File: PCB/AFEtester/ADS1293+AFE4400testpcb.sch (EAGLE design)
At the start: 47 parts, among them IC1 ADS1293, J1 POWER_JACK, U2 TPS61093DSKT, Y1 4.096MHz

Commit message: afe4400 pcb stuff
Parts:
- added 3V3-POWER-TESTPOINT1, 3V3-POWER-TESTPOINT2: (no value), SparkFun-Connectors:CONN_02
- added C16: 1nF, SparkFun-Capacitors:1.0NF/1000PF-0603-50V-10%
- added C17, C18, C19, C20, C22, C23, C24: 10uF, SparkFun-Retired:10UF-TANT
- added C21, C27: 10nF, SparkFun-Capacitors:10NF-0603-50V-10%
- added C25, C29, C30: 0.1uF, SparkFun-Capacitors:0.1UF-0603-25V-5%
- added C26: 1.0uF, SparkFun-Capacitors:1.0UF-0805-25V-10%
- added C28, C31: 2.2uF, SparkFun-Capacitors:2.2UF-0805-25V-(+80/-20%)
- added C32, C33: 18pF, SparkFun-Capacitors:18PF-0603-50V-5%
- added D1: GREEN, SparkFun-LED:LED-GREEN1206
- added D2, D3: BAV99S, nxp_60:BAV99S
- added FRAME2: FRAME-LEDGER, SparkFun-Aesthetics:FRAME-LEDGER
- added IC2: LP3878MR-ADJ_NOPB, LP3878MR-ADJ_NOPB:LP3878MR-ADJ_NOPB
- added J3: (no value), SparkFun-Connectors:DB9FEMALE
- added J4: (no value), SparkFun-Connectors:CONN_08"
- added J5: (no value), SparkFun-Connectors:CONN_04
- added L2, L3, L4: 3.3µH/±20%/450mA, SparkFun-Coils:INDUCTOR-0805-3.3UH
- added R18, R29: 1k, SparkFun-Resistors:1KOHM-0603-1/10W-1%
- added R19: 4.7k, SparkFun-Resistors:4.7KOHM-0603-1/10W-1%
- added R20, R21, R24, R25, R26, R27, R28, R30, R31, R32, R33, R34, R35: 0, SparkFun-Resistors:0OHM-0603-1/10W-5%
- added R22: 75k, SparkFun-Resistors:75KOHM-0603-1/10W-1%
- added R23: 47k, SparkFun-Resistors:47KOHM-0603-1/10W-1%
- added R36: 10, SparkFun-Resistors:10OHM-0603-1/10W-1%
- added R37: 10k, SparkFun-Resistors:10KOHM-0603-1/10W-1%
- added R38, R39, R40, R41, R42, R43: 130, SparkFun-Resistors:330OHM-0603-1/10W-1%
- added S2: MOMENTARY-SWITCH-SPST-PTH-6.0MM, SparkFun-Switches:MOMENTARY-SWITCH-SPST-PTH-6.0MM
- added U3: AFE4400_RHA_40, AFE4400:AFE4400_RHA_40
- added Y2: 8MHz, SparkFun-Clocks:CRYSTAL-8MHZSMD-5X3.2
- C13: device SparkFun-Capacitors:10UF-0805-10V-10% -> SparkFun-Retired:10UF-TANT
- C14, C15: value 0.1uF -> 10nF; device SparkFun-Capacitors:0.1UF-0603-25V-(+80/-20%) -> SparkFun-Capacitors:10NF-0603-50V-10%
- L1: value LPS3010-102MRC -> 3.3µH/±20%/450mA; device LPS3010-102MRC:LPS3010-102MRC -> SparkFun-Coils:INDUCTOR-0805-3.3UH
- R17: value 0 -> 2.55k; device SparkFun-Resistors:0OHM-0603-1/10W-5% -> SparkFun-Resistors:2.55KOHM-0603-1/10W-1%
- U2: value TPS61093DSKT -> TPS7A4901DGNR; device Texas Instruments_By_element14_Batch_1:TPS61093DSKT -> Texas Instruments_By_element14_Batch_1:TPS7A4901DGNR
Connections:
- removed net C: COMM-CONN.6, IC1.SCLK
- removed net VCC: C13.1, R16.1
- new net ADC_RDY: J4.5, U3.ADC_RDY
- new net AFE_PDN: J4.8, U3.AFE_*PDN
- new net CLKOUT_AFE: J4.2, R36.2
- new net DIAG_END: J4.7, U3.DIAG_END
- new net LED_ALM: J4.6, U3.LED_ALM
- new net LED_DRV_SUP: C26.1, D3-1.K2, D3-2.K2, J5.1, R20.2, U3.LED_DRV_SUP, U3.LED_DRV_SUP_2
- new net N$21: 3V3-POWER-TESTPOINT1.2, C16.1, IC2.OUT, R17.2
- new net N$22: C14.1, U2.NR/SS
- new net N$23: C19.+, L1.2, R20.1
- new net N$24: C20.+, L2.2, R21.1
- new net N$25: C13.+, R26.1, U2.EN, U2.IN
- new net N$26: 3V3-POWER-TESTPOINT2.2, C21.1, R22.2, U2.OUT
- new net N$27: C21.2, R22.1, R23.2, U2.FB
- new net N$28: C23.+, L3.2, R27.1
- new net N$29: C17.+, IC2.!SHUTDOWN, IC2.IN, R25.1
- new net N$30: C24.+, L4.2, R28.1
- new net N$31: C28.2, U3.BG
- new net N$32: C31.1, U3.TX_REF
- new net N$33: R32.2, U3.TXN
- new net N$34: R29.2, U3.VCM
- new net N$36: R31.2, U3.INN
- new net N$37: R30.2, U3.INP
- new net N$38: D2-2.K1A2, J3.5, R31.1
- new net N$39: D2-1.K1A2, J3.9, R30.1
- new net N$40: R33.2, U3.TXP
- new net N$41: D3-1.K1A2, J3.3, R32.1
- new net N$42: D3-2.K1A2, J3.2, R33.1
- new net N$43: C32.2, R34.2, Y2.1
- new net N$44: C33.1, R35.1, Y2.2
- new net N$45: R36.1, U3.CLKOUT
- new net N$46: R37.2, S2.2, U3.*RESET
- new net N$48: R35.2, U3.XOUT
- new net N$49: R38.1, U3.DNC
- new net N$50: R42.1, U3.DNC_2
- new net N$52: R41.1, U3.DNC_3
- new net N$53: R40.1, U3.DNC_4
- new net N$54: R39.1, U3.DNC_5
- new net N$55: R38.2
- new net N$56: R39.2
- new net N$57: R40.2
- new net N$58: R41.2
- new net N$59: R42.2
- new net PD_ALM: J4.4, U3.PD_ALM
- new net RX_ANA_SUP: C30.1, D2-1.K2, D2-2.K2, J5.4, R28.2, U3.RX_ANA_SUP, U3.RX_ANA_SUP_2
- new net RX_DIG_SUP: C29.1, J5.3, R27.2, R37.1, U3.RX_DIG_SUP
- new net RX_SUP: 3V3-POWER-TESTPOINT2.1, C22.+, L3.1, L4.1
- new net SCLK: COMM-CONN.6, IC1.SCLK, U3.SCLK
- new net STE: J4.1, U3.SPISTE
- new net TX_CTRL_SUP: C25.1, J5.2, R21.2, U3.TX_CTRL_SUP
- new net VCM_SHIELD: C27.1, R29.1
- new net XIN_MSP: J4.3, R34.1, U3.XIN
- net +5V: now also D1.A, R25.2, R26.2
- net GND: now also C13.-, C14.2, C15.2, C17.-, C18.-, C19.-, C20.-, C22.-, C23.-, C24.-, C25.2, C26.2, C27.2, C28.1, C29.2, C30.2, C31.2, C32.1, C33.2, D2-1.A1, D2-2.A1, D3-1.A1, D3-2.A1, IC2.EP, IC2.GND, IC2.NC_1, J3.7, R16.1, R16.2, R18.1, R19.1, R23.1, R24.1, R24.2, R43.1, S2.1, U2.EP, U3.EPAD, U3.LED_DRV_GND, U3.LED_DRV_GND_2, U3.LED_DRV_GND_3, U3.RX_ANA_GND, U3.RX_ANA_GND_2, U3.RX_ANA_GND_3, U3.RX_DIG_GND, U3.RX_DIG_GND_2, U3.VSS; no longer C13.2
- net MISO: now also U3.SPISOMI
- net MOSI: now also U3.SPISIMO
- net N$18: now also 3V3-POWER-TESTPOINT1.1, C18.+, L1.1, L2.1; no longer R17.2, U2.EN
- net N$19: now also C16.2, IC2.ADJ, R18.2; no longer R16.2, U2.VIN
- net N$20: now also C15.1, IC2.BYP; no longer C15.2, U2.CP2
- net N$4: now also D1.C, R19.2; no longer C15.1, U2.CP1
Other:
- note added: "2.7kR will be better"
- note added: "we can also try 1uH"
- moved on the sheet: C14, C15, R16, R17

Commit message: almost complete AFE PCB
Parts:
- removed FRAME2: FRAME-LEDGER, SparkFun-Aesthetics:FRAME-LEDGER
- J5: device SparkFun-Connectors:CONN_04 -> SparkFun-Connectors:CONN_05
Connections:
- net GND: now also J5.5; no longer R43.1
- net LED_DRV_SUP: now also J5.3; no longer J5.1
- net N$31: now also R43.1
- net RX_ANA_SUP: now also J5.1; no longer J5.4
- net RX_DIG_SUP: now also J5.2; no longer J5.3
- net TX_CTRL_SUP: now also J5.4; no longer J5.2
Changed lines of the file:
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@@
 <part name="SUPPLY32" library="supply2" library_urn="urn:adsk.eagle:library:372" deviceset="GND" device=""/>
 <part name="R43" library="SparkFun-Resistors" deviceset="330OHM" device="-0603-1/10W-1%" value="130"/>
-<part name="FRAME2" library="SparkFun-Aesthetics" deviceset="FRAME-LEDGER" device=""/>
 <part name="J4" library="SparkFun-Connectors" deviceset="CONN_08" device="&quot;"/>
-<part name="J5" library="SparkFun-Connectors" deviceset="CONN_04" device=""/>
+<part name="J5" library="SparkFun-Connectors" deviceset="CONN_05" device=""/>
+<part name="SUPPLY33" library="supply2" library_urn="urn:adsk.eagle:library:372" deviceset="GND" device=""/>
 </parts>
 <sheets>
@@
 <instance part="SUPPLY32" gate="GND" x="320.04" y="53.34"/>
 <instance part="R43" gate="G$1" x="447.04" y="106.68"/>
-<instance part="FRAME2" gate="G$1" x="294.64" y="2.54"/>
-<instance part="FRAME2" gate="G$2" x="624.84" y="2.54"/>
 <instance part="J4" gate="G$1" x="576.58" y="251.46"/>
-<instance part="J5" gate="G$1" x="576.58" y="208.28"/>
+<instance part="J5" gate="G$1" x="576.58" y="210.82"/>
+<instance part="SUPPLY33" gate="GND" x="594.36" y="220.98"/>
 </instances>
 <busses>
@@
 <pinref part="SUPPLY23" gate="GND" pin="GND"/>
 <wire x1="441.96" y1="101.6" x2="449.58" y2="101.6" width="0.1524" layer="91"/>
-<wire x1="441.96" y1="101.6" x2="441.96" y2="106.68" width="0.1524" layer="91"/>
-<junction x="441.96" y="101.6"/>
-<pinref part="R43" gate="G$1" pin="1"/>
 </segment>
 <segment>
@@
 <wire x1="320.04" y1="68.58" x2="320.04" y2="55.88" width="0.1524" layer="91"/>
 <pinref part="SUPPLY32" gate="GND" pin="GND"/>
+</segment>
+<segment>
+<pinref part="J5" gate="G$1" pin="5"/>
+<wire x1="584.2" y1="215.9" x2="586.74" y2="215.9" width="0.1524" layer="91"/>
+<wire x1="586.74" y1="215.9" x2="586.74" y2="226.06" width="0.1524" layer="91"/>
+<wire x1="586.74" y1="226.06" x2="594.36" y2="226.06" width="0.1524" layer="91"/>
+<pinref part="SUPPLY33" gate="GND" pin="GND"/>
+<wire x1="594.36" y1="226.06" x2="594.36" y2="223.52" width="0.1524" layer="91"/>
 </segment>
 </net>
@@
 </segment>
 <segment>
-<pinref part="J5" gate="G$1" pin="1"/>
-<wire x1="581.66" y1="205.74" x2="586.74" y2="205.74" width="0.1524" layer="91"/>
-<label x="586.74" y="205.74" size="1.778" layer="95" xref="yes"/>
+<pinref part="J5" gate="G$1" pin="3"/>
+<wire x1="584.2" y1="210.82" x2="596.9" y2="210.82" width="0.1524" layer="91"/>
+<label x="596.9" y="210.82" size="1.778" layer="95" xref="yes"/>
 </segment>
 </net>
@@
 </segment>
 <segment>
-<pinref part="J5" gate="G$1" pin="2"/>
-<wire x1="581.66" y1="208.28" x2="586.74" y2="208.28" width="0.1524" layer="91"/>
-<label x="586.74" y="208.28" size="1.778" layer="95" xref="yes"/>
+<pinref part="J5" gate="G$1" pin="4"/>
+<wire x1="584.2" y1="213.36" x2="596.9" y2="213.36" width="0.1524" layer="91"/>
+<label x="596.9" y="213.36" size="1.778" layer="95" xref="yes"/>
 </segment>
 </net>
@@
 </segment>
 <segment>
-<pinref part="J5" gate="G$1" pin="3"/>
-<wire x1="581.66" y1="210.82" x2="586.74" y2="210.82" width="0.1524" layer="91"/>
-<label x="586.74" y="210.82" size="1.778" layer="95" xref="yes"/>
+<pinref part="J5" gate="G$1" pin="2"/>
+<wire x1="584.2" y1="208.28" x2="596.9" y2="208.28" width="0.1524" layer="91"/>
+<label x="596.9" y="208.28" size="1.778" layer="95" xref="yes"/>
 </segment>
 </net>
@@
 </segment>
 <segment>
-<pinref part="J5" gate="G$1" pin="4"/>
-<wire x1="581.66" y1="213.36" x2="586.74" y2="213.36" width="0.1524" layer="91"/>
-<label x="586.74" y="213.36" size="1.778" layer="95" xref="yes"/>
+<pinref part="J5" gate="G$1" pin="1"/>
+<wire x1="584.2" y1="205.74" x2="596.9" y2="205.74" width="0.1524" layer="91"/>
+<label x="596.9" y="205.74" size="1.778" layer="95" xref="yes"/>
 </segment>
 </net>
@@
 <pinref part="C28" gate="G$1" pin="2"/>
 <wire x1="447.04" y1="93.98" x2="441.96" y2="93.98" width="0.1524" layer="91"/>
-</segment>
-</net>
+<pinref part="R43" gate="G$1" pin="1"/>
+<wire x1="441.96" y1="106.68" x2="436.88" y2="106.68" width="0.1524" layer="91"/>
+<wire x1="436.88" y1="106.68" x2="436.88" y2="93.98" width="0.1524" layer="91"/>
+<wire x1="436.88" y1="93.98" x2="441.96" y2="93.98" width="0.1524" layer="91"/>
+<junction x="441.96" y="93.98"/>
+</segment>
+</net>

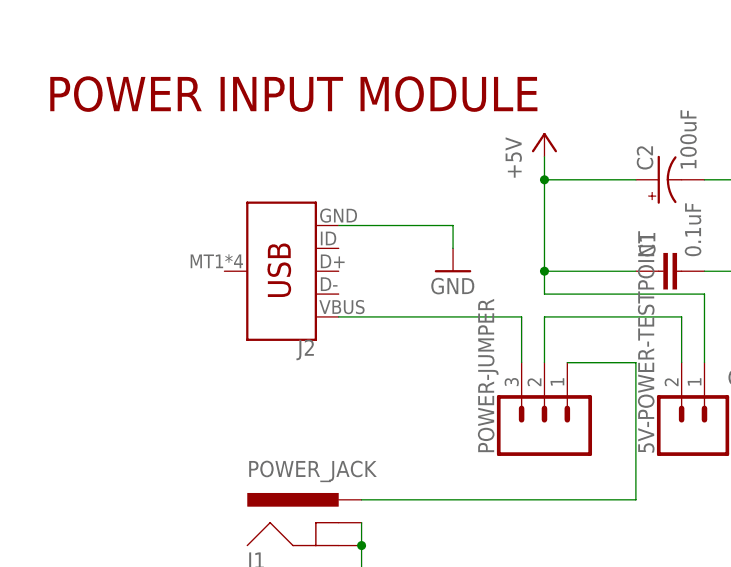
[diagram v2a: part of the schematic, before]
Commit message: Finishing ADS&AFE joint test pcb
exporting gerber
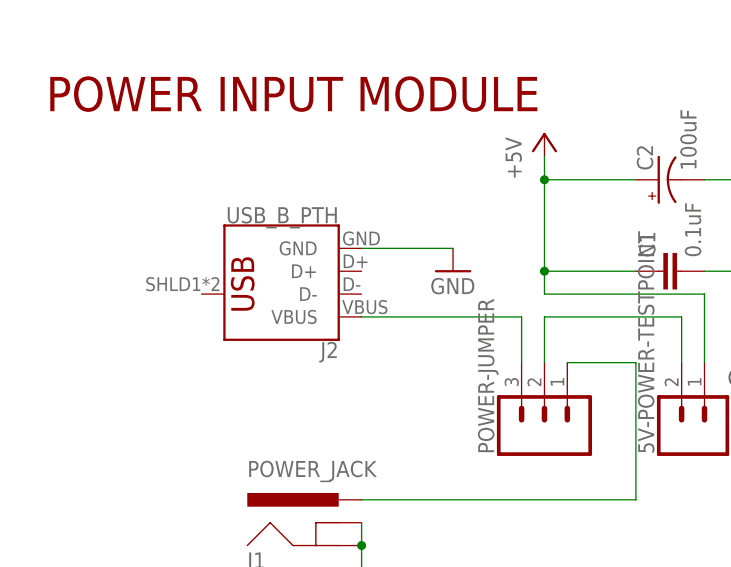
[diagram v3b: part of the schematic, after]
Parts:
- J2: value (none) -> USB_B_PTH; device SparkFun-Connectors:USB_MICRO-B_SMT -> SparkFun-Connectors:USB_B_PTH
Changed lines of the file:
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@@
 <part name="GND1" library="supply1" library_urn="urn:adsk.eagle:library:371" deviceset="GND" device=""/>
 <part name="C1" library="SparkFun-Capacitors" deviceset="0.1UF" device="-0603-25V-(+80/-20%)" value="0.1uF"/>
-<part name="J2" library="SparkFun-Connectors" deviceset="USB_MICRO-B" device="_SMT"/>
+<part name="J2" library="SparkFun-Connectors" deviceset="USB_B" device="_PTH"/>
 <part name="GND2" library="supply1" library_urn="urn:adsk.eagle:library:371" deviceset="GND" device=""/>
 <part name="POWER-JUMPER" library="SparkFun-Connectors" deviceset="CONN_03" device=""/>
@@
 <segment>
 <pinref part="J2" gate="G$1" pin="GND"/>
-<wire x1="40.64" y1="165.1" x2="53.34" y2="165.1" width="0.1524" layer="91"/>
+<wire x1="43.18" y1="162.56" x2="53.34" y2="162.56" width="0.1524" layer="91"/>
 <pinref part="GND2" gate="1" pin="GND"/>
-<wire x1="53.34" y1="165.1" x2="53.34" y2="162.56" width="0.1524" layer="91"/>
 </segment>
 <segment>
@@
 <segment>
 <pinref part="J2" gate="G$1" pin="VBUS"/>
-<wire x1="40.64" y1="154.94" x2="60.96" y2="154.94" width="0.1524" layer="91"/>
+<wire x1="43.18" y1="154.94" x2="60.96" y2="154.94" width="0.1524" layer="91"/>
 <pinref part="POWER-JUMPER" gate="J$1" pin="3"/>
 <wire x1="60.96" y1="154.94" x2="60.96" y2="149.86" width="0.1524" layer="91"/>
